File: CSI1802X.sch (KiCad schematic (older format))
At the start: 6 parts

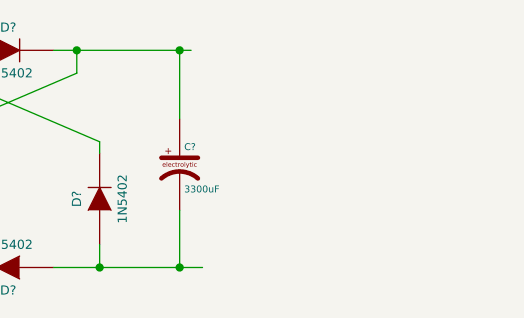
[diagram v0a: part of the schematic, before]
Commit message: pulling in resistors lib
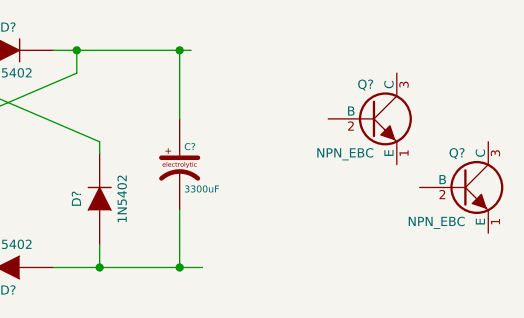
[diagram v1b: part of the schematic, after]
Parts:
- added Q? (x2): NPN_EBC, ~, symbol NPN_EBC
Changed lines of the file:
@@
 EESchema Schematic File Version 2
+LIBS:resistors_PL
 LIBS:transistors_PL
 LIBS:capacitors_PL
@@
 	4000 3750 4000 4000
 Connection ~ 4000 4000
+$Comp
+L NPN_EBC Q?
+U 1 1 533A0F94
+P 4850 3350
+F 0 "Q?" H 4850 3500 40  0000 R CNN
+F 1 "NPN_EBC" H 4850 3200 40  0000 R CNN
+F 2 "~" H 4850 3350 60  0000 C CNN
+F 3 "~" H 4850 3350 60  0000 C CNN
+	1    4850 3350
+	1    0    0    -1
+$EndComp
+$Comp
+L NPN_EBC Q?
+U 1 1 533A0FA1
+P 5250 3650
+F 0 "Q?" H 5250 3800 40  0000 R CNN
+F 1 "NPN_EBC" H 5250 3500 40  0000 R CNN
+F 2 "~" H 5250 3650 60  0000 C CNN
+F 3 "~" H 5250 3650 60  0000 C CNN
+	1    5250 3650
+	1    0    0    -1
+$EndComp
 $EndSCHEMATC

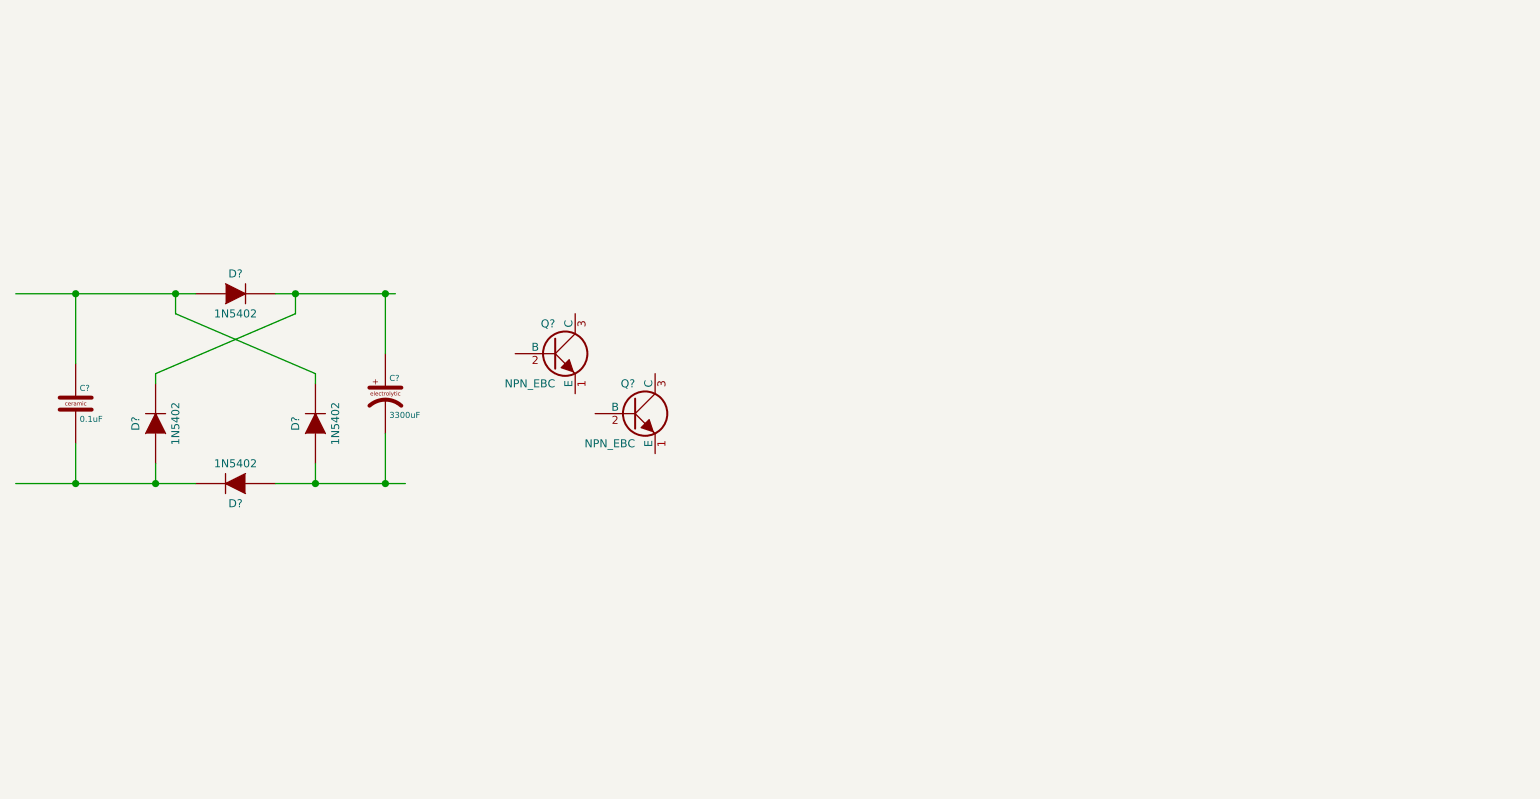
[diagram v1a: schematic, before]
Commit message: setting up pass transistor
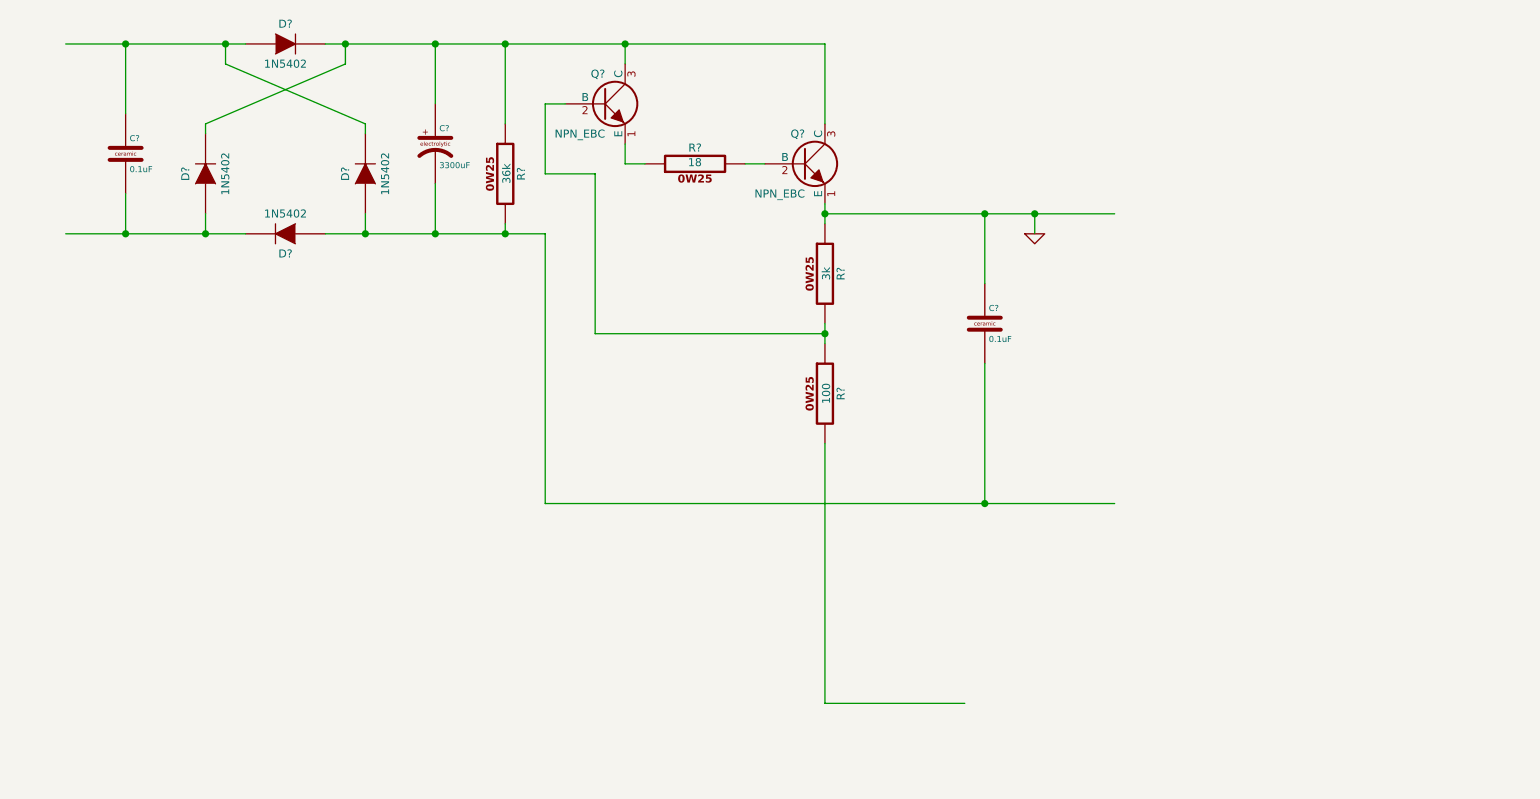
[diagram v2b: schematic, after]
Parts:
- added C?: 0.1uF, ~, symbol C_CER
- added R?: 36k, ~, symbol R_0W25
- added R?: 18, ~, symbol R_0W25
- added R?: 3k, ~, symbol R_0W25
- added R?: 100, ~, symbol R_0W25
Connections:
- net labels added: GND
- wire segments 16 -> 38
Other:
- moved on the sheet: C?, D?, Q?

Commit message: op amp voltage control
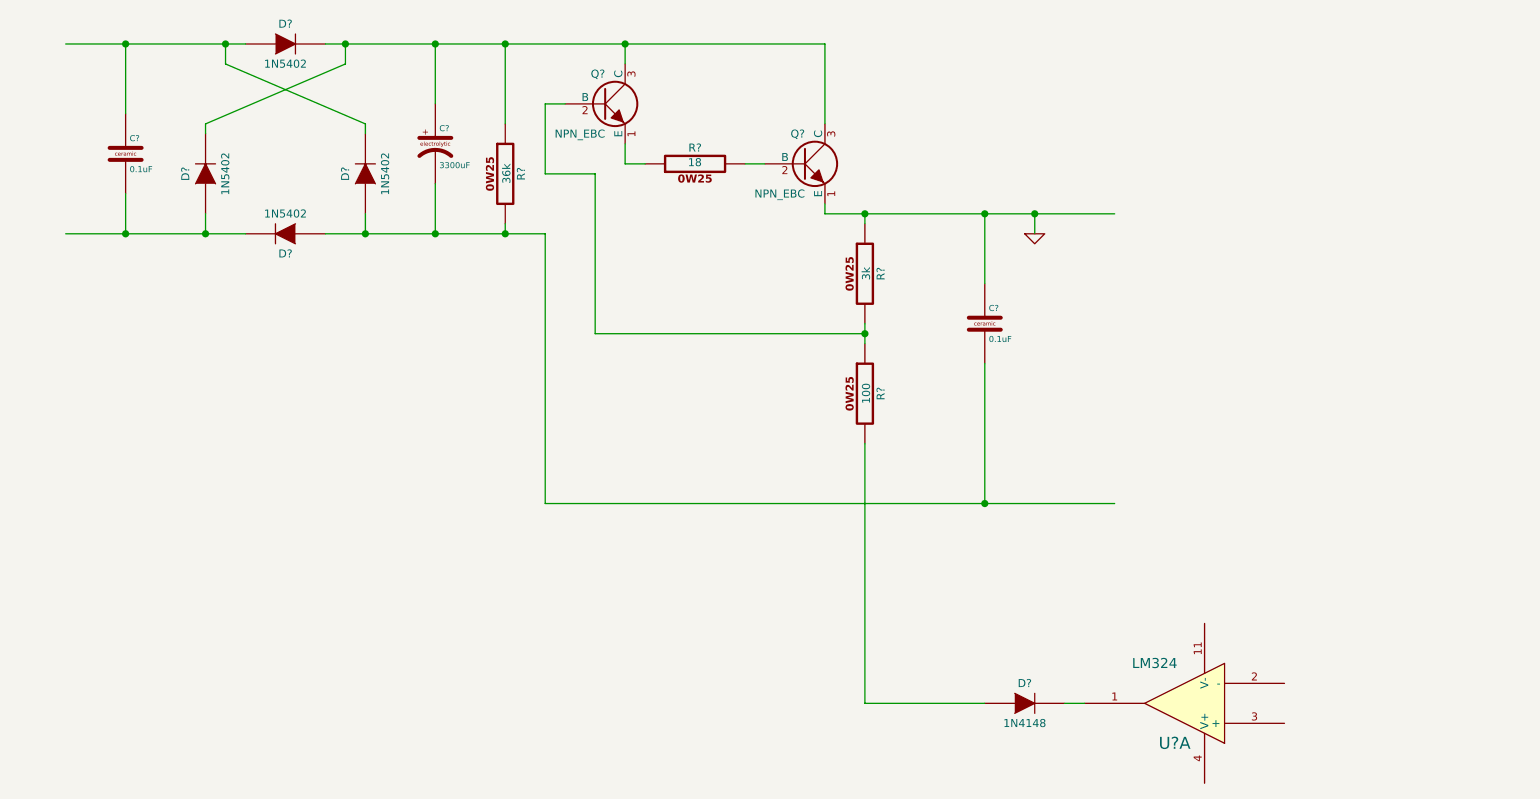
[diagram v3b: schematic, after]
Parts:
- added D?: 1N4148, ~, symbol DIODE
- added U?: LM324, symbol LM324
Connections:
- wire segments 38 -> 40
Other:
- moved on the sheet: R?
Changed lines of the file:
@@
 $EndComp
 Wire Wire Line
-	4250 2100 4250 1800
+	4250 1800 4250 2100
 Connection ~ 4250 1800
 Wire Wire Line
@@
 Connection ~ 4600 1800
 Wire Wire Line
-	5200 1900 5200 1800
+	5200 1800 5200 1900
 Connection ~ 5200 1800
 $Comp
@@
 L R_0W25 R?
 U 1 1 533A11D4
-P 6200 2950
-F 0 "R?" V 6280 2950 40  0000 C CNN
-F 1 "3k" V 6207 2951 40  0000 C CNN
-F 2 "~" V 6130 2950 30  0000 C CNN
-F 3 "~" H 6200 2950 30  0000 C CNN
-	1    6200 2950
+P 6400 2950
+F 0 "R?" V 6480 2950 40  0000 C CNN
+F 1 "3k" V 6407 2951 40  0000 C CNN
+F 2 "~" V 6330 2950 30  0000 C CNN
+F 3 "~" H 6400 2950 30  0000 C CNN
+	1    6400 2950
 	1    0    0    -1
 $EndComp
@@
 L R_0W25 R?
 U 1 1 533A11E3
-P 6200 3550
-F 0 "R?" V 6280 3550 40  0000 C CNN
-F 1 "100" V 6207 3551 40  0000 C CNN
-F 2 "~" V 6130 3550 30  0000 C CNN
-F 3 "~" H 6200 3550 30  0000 C CNN
-	1    6200 3550
+P 6400 3550
+F 0 "R?" V 6480 3550 40  0000 C CNN
+F 1 "100" V 6407 3551 40  0000 C CNN
+F 2 "~" V 6330 3550 30  0000 C CNN
+F 3 "~" H 6400 3550 30  0000 C CNN
+	1    6400 3550
 	1    0    0    -1
 $EndComp
 Wire Wire Line
-	6200 2600 6200 2700
-Wire Wire Line
 	6200 2650 7650 2650
-Connection ~ 6200 2650
-Wire Wire Line
-	6200 3200 6200 3300
 $Comp
 L C_CER C?
@@
 Connection ~ 7250 2650
 Wire Wire Line
-	6200 3800 6200 5100
-Wire Wire Line
-	6200 5100 6900 5100
-Wire Wire Line
-	6200 3250 5050 3250
+	5050 3250 6400 3250
 Wire Wire Line
 	5050 3250 5050 2450
@@
 Wire Wire Line
 	4800 2100 4900 2100
-Connection ~ 6200 3250
+$Comp
+L LM324 U?
+U 1 1 533A1511
+P 8000 5100
+F 0 "U?" H 8050 5300 60  0000 C CNN
+F 1 "LM324" H 8150 4900 50  0000 C CNN
+F 2 "" H 8000 5100 60  0000 C CNN
+F 3 "" H 8000 5100 60  0000 C CNN
+	1    8000 5100
+	-1   0    0    1
+$EndComp
+$Comp
+L DIODE D?
+U 1 1 533A1528
+P 7200 5100
+F 0 "D?" H 7200 5200 40  0000 C CNN
+F 1 "1N4148" H 7200 5000 40  0000 C CNN
+F 2 "~" H 7200 5100 60  0000 C CNN
+F 3 "~" H 7200 5100 60  0000 C CNN
+	1    7200 5100
+	1    0    0    -1
+$EndComp
+Wire Wire Line
+	7400 5100 7500 5100
+Wire Wire Line
+	6400 2650 6400 2700
+Connection ~ 6400 2650
+Wire Wire Line
+	6400 3200 6400 3300
+Wire Wire Line
+	6200 2650 6200 2600
+Connection ~ 6400 3250
+Wire Wire Line
+	6400 3800 6400 5100
+Wire Wire Line
+	6400 5100 7000 5100
 $EndSCHEMATC

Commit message: 5V positive rail
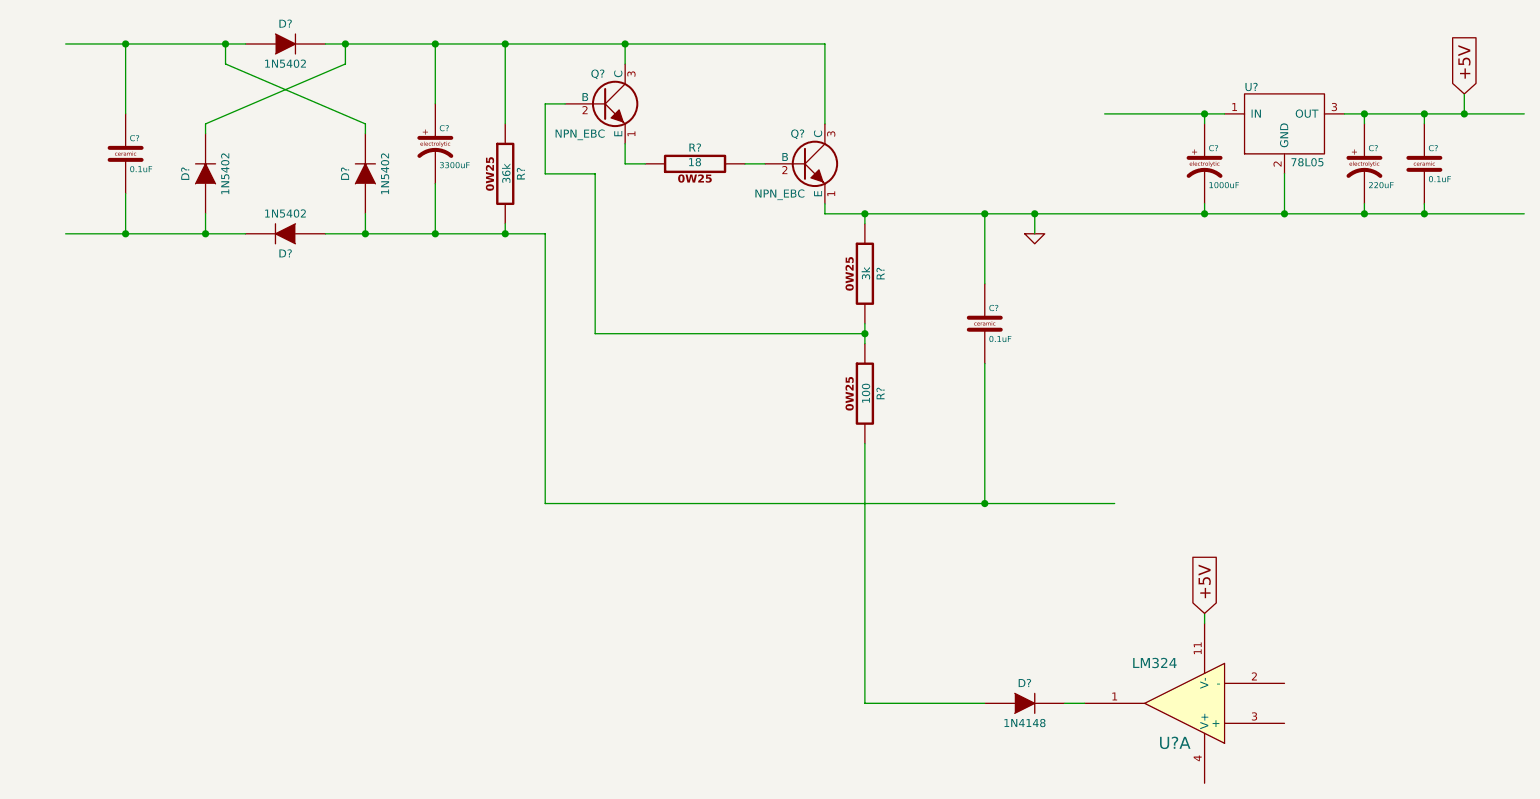
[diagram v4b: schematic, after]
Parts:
- added C?: 1000uF, ~, symbol C_EL
- added C?: 220uF, ~, symbol C_EL
- added C?: 0.1uF, ~, symbol C_CER
- added U?: 78L05, ~, symbol 78L05
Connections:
- net labels added: +5V
- wire segments 40 -> 51
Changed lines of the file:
@@
 EESchema Schematic File Version 2
+LIBS:regulators_PL
 LIBS:resistors_PL
 LIBS:transistors_PL
@@
 $EndComp
 Wire Wire Line
-	6200 2650 7650 2650
+	6200 2650 9700 2650
 $Comp
 L C_CER C?
@@
 Wire Wire Line
 	6400 5100 7000 5100
+$Comp
+L 78L05 U?
+U 1 1 533A185C
+P 8500 2200
+F 0 "U?" H 8300 2360 40  0000 L BNN
+F 1 "78L05" H 8700 2030 40  0000 R TNN
+F 2 "~" H 8500 2200 60  0000 C CNN
+F 3 "~" H 8500 2200 60  0000 C CNN
+	1    8500 2200
+	1    0    0    -1
+$EndComp
+$Comp
+L C_EL C?
+U 1 1 533A186B
+P 8100 2400
+F 0 "C?" H 8120 2460 30  0000 L BNN
+F 1 "1000uF" H 8120 2310 30  0000 L TNN
+F 2 "~" H 8138 2250 30  0000 C CNN
+F 3 "~" H 8100 2400 60  0000 C CNN
+	1    8100 2400
+	1    0    0    -1
+$EndComp
+$Comp
+L C_EL C?
+U 1 1 533A187A
+P 8900 2400
+F 0 "C?" H 8920 2460 30  0000 L BNN
+F 1 "220uF" H 8920 2310 30  0000 L TNN
+F 2 "~" H 8938 2250 30  0000 C CNN
+F 3 "~" H 8900 2400 60  0000 C CNN
+	1    8900 2400
+	1    0    0    -1
+$EndComp
+$Comp
+L C_CER C?
+U 1 1 533A1889
+P 9200 2400
+F 0 "C?" H 9220 2460 30  0000 L BNN
+F 1 "0.1uF" H 9220 2340 30  0000 L TNN
+F 2 "~" H 9238 2250 30  0000 C CNN
+F 3 "~" H 9200 2400 60  0000 C CNN
+	1    9200 2400
+	1    0    0    -1
+$EndComp
+Wire Wire Line
+	8800 2150 9700 2150
+Wire Wire Line
+	9200 2200 9200 2150
+Connection ~ 9200 2150
+Wire Wire Line
+	8900 2200 8900 2150
+Connection ~ 8900 2150
+Wire Wire Line
+	8900 2600 8900 2650
+Connection ~ 8900 2650
+Wire Wire Line
+	9200 2600 9200 2650
+Connection ~ 9200 2650
+Wire Wire Line
+	8500 2450 8500 2650
+Connection ~ 8500 2650
+Wire Wire Line
+	7600 2150 8200 2150
+Wire Wire Line
+	8100 2200 8100 2150
+Connection ~ 8100 2150
+Wire Wire Line
+	8100 2600 8100 2650
+Connection ~ 8100 2650
+Text GLabel 9400 2050 1    60   Input ~ 0
++5V
+Wire Wire Line
+	9400 2150 9400 2050
+Connection ~ 9400 2150
+Text GLabel 8100 4650 1    60   Input ~ 0
++5V
+Wire Wire Line
+	8100 4700 8100 4650
 $EndSCHEMATC
